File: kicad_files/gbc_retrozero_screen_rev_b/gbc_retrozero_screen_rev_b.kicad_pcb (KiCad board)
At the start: 2 copper layers, 70.1 x 64.8 mm, 25 parts, among them J1 Raspberry_Pi_2_3, SW1 SW_Push_SPDT, U1 2.4_screen_ribbon, U2 gbc_just_button_connector, U3 gbc_power_connector, U4 sound_pot_5pin, U5 gbc_l_and_r_3pin, U6 pam8403, U7 usb_c_6pin, U8 gbc_l_and_r_1pin

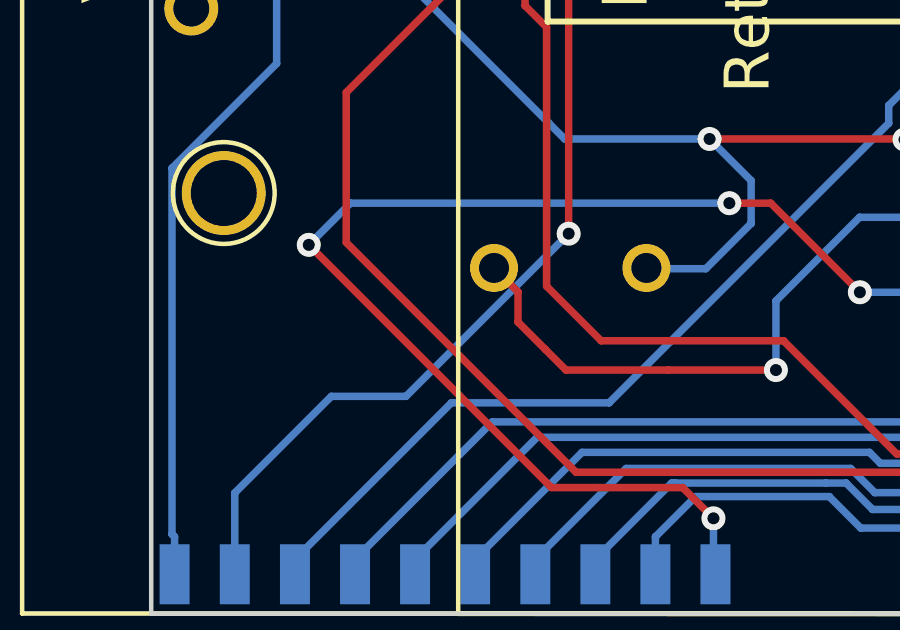
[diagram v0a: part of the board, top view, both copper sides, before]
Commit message: fixed issus with J1-PAD36 and trace
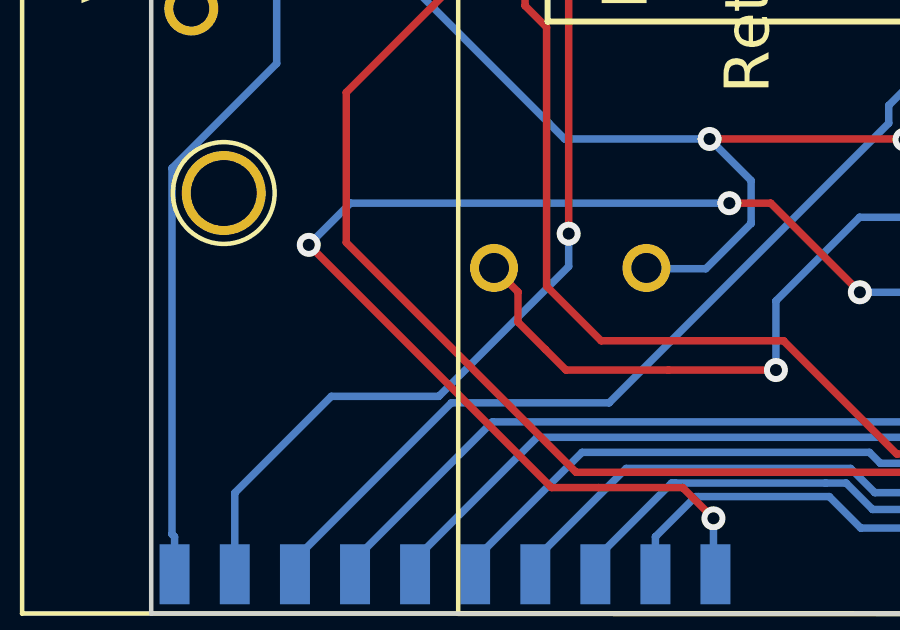
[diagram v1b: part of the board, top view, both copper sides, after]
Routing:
- net Net-(J1-Pad11): track 57.4 -> 58.0 mm
